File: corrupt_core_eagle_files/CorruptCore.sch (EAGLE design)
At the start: 90 parts, among them K1 DTS-3, K10 DTS-3, K11 DTS-3, K12 DTS-3, K13 DTS-3, K14 DTS-3, K15 DTS-3, K16 DTS-3, K2 DTS-3, K3 DTS-3, K4 DTS-3, K5 DTS-3, K6 DTS-3, K7 DTS-3, K8 DTS-3, K9 DTS-3, T1 TRANS_NPN-MMBTA42, T2 TRANS_NPN-MMBTA42, T3 TRANS_NPN-MMBTA42, T4 TRANS_NPN-MMBTA42, U1 MEGA8-P, U2 SNX4HC595SOIC16, U3 SNX4HC595SOIC16, U4 SNX4HC595SOIC16, U5 ULN2803ASOIC18, U6 ULN2803ASOIC18, U7 ULN2803ASOIC18, U8 LTC1799, Y1 16MHz

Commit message: -routed everything
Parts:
- added DUMMY@PROG: DUMMY, wirepad:1,6/0,8
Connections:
- net GND: now also DUMMY@PROG.P
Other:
- moved on the sheet: 5V@POT1, 5V@POT2, 5V@POT3, GND@POT1, GND@POT2, GND@POT3, POT1, POT2, POT3, RESET, RX, TX
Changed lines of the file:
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@@
 <part name="CPT1" library="wirepad" library_urn="urn:adsk.eagle:library:412" deviceset="1,6/0,8" device=""/>
 <part name="P+17" library="supply1" library_urn="urn:adsk.eagle:library:371" deviceset="+5V" device=""/>
+<part name="DUMMY@PROG" library="wirepad" library_urn="urn:adsk.eagle:library:412" deviceset="1,6/0,8" device="" value="DUMMY"/>
+<part name="GND17" library="supply1" library_urn="urn:adsk.eagle:library:371" deviceset="GND" device=""/>
 </parts>
 <sheets>
@@
 <instance part="GND34" gate="1" x="-10.16" y="35.56"/>
 <instance part="P+10" gate="1" x="7.62" y="43.18"/>
-<instance part="TX" gate="P" x="35.56" y="-33.02" rot="R180"/>
-<instance part="RX" gate="P" x="35.56" y="-38.1" rot="R180"/>
-<instance part="RESET" gate="P" x="35.56" y="-43.18" rot="R180"/>
+<instance part="TX" gate="P" x="35.56" y="-35.56" rot="R180"/>
+<instance part="RX" gate="P" x="35.56" y="-40.64" rot="R180"/>
+<instance part="RESET" gate="P" x="35.56" y="-45.72" rot="R180"/>
 <instance part="5V@PROG" gate="P" x="43.18" y="-30.48"/>
 <instance part="GND@PROG" gate="P" x="43.18" y="-40.64"/>
 <instance part="GND35" gate="1" x="60.96" y="-40.64" rot="R90"/>
 <instance part="P+11" gate="1" x="60.96" y="-30.48" rot="R270"/>
-<instance part="GND@POT1" gate="P" x="15.24" y="-55.88"/>
-<instance part="5V@POT1" gate="P" x="15.24" y="-60.96"/>
-<instance part="POT1" gate="P" x="15.24" y="-66.04"/>
-<instance part="GND@POT2" gate="P" x="43.18" y="-55.88"/>
-<instance part="5V@POT2" gate="P" x="43.18" y="-60.96"/>
-<instance part="POT2" gate="P" x="43.18" y="-66.04"/>
-<instance part="POT3" gate="P" x="71.12" y="-66.04"/>
-<instance part="5V@POT3" gate="P" x="71.12" y="-60.96"/>
-<instance part="GND@POT3" gate="P" x="71.12" y="-55.88"/>
-<instance part="GND36" gate="1" x="86.36" y="-55.88" rot="R90"/>
-<instance part="GND37" gate="1" x="58.42" y="-55.88" rot="R90"/>
-<instance part="GND38" gate="1" x="30.48" y="-55.88" rot="R90"/>
-<instance part="P+12" gate="1" x="93.98" y="-60.96" rot="R270"/>
-<instance part="P+13" gate="1" x="66.04" y="-60.96" rot="R270"/>
-<instance part="P+14" gate="1" x="38.1" y="-60.96" rot="R270"/>
+<instance part="GND@POT1" gate="P" x="15.24" y="-63.5"/>
+<instance part="5V@POT1" gate="P" x="15.24" y="-68.58"/>
+<instance part="POT1" gate="P" x="15.24" y="-73.66"/>
+<instance part="GND@POT2" gate="P" x="43.18" y="-63.5"/>
+<instance part="5V@POT2" gate="P" x="43.18" y="-68.58"/>
+<instance part="POT2" gate="P" x="43.18" y="-73.66"/>
+<instance part="POT3" gate="P" x="71.12" y="-73.66"/>
+<instance part="5V@POT3" gate="P" x="71.12" y="-68.58"/>
+<instance part="GND@POT3" gate="P" x="71.12" y="-63.5"/>
+<instance part="GND36" gate="1" x="86.36" y="-63.5" rot="R90"/>
+<instance part="GND37" gate="1" x="58.42" y="-63.5" rot="R90"/>
+<instance part="GND38" gate="1" x="30.48" y="-63.5" rot="R90"/>
+<instance part="P+12" gate="1" x="93.98" y="-68.58" rot="R270"/>
+<instance part="P+13" gate="1" x="66.04" y="-68.58" rot="R270"/>
+<instance part="P+14" gate="1" x="38.1" y="-68.58" rot="R270"/>
 <instance part="T1" gate="G$1" x="276.86" y="-38.1" rot="MR180"/>
 <instance part="T2" gate="G$1" x="276.86" y="-5.08" rot="MR180"/>
@@
 <instance part="CPT1" gate="P" x="330.2" y="-43.18" rot="R270"/>
 <instance part="P+17" gate="1" x="330.2" y="-50.8" rot="MR180"/>
+<instance part="DUMMY@PROG" gate="P" x="43.18" y="-50.8"/>
+<instance part="GND17" gate="1" x="60.96" y="-50.8" rot="R90"/>
 </instances>
 <busses>
@@
 <segment>
 <pinref part="5V@POT3" gate="P" pin="P"/>
-<wire x1="73.66" y1="-60.96" x2="91.44" y2="-60.96" width="0.1524" layer="91"/>
+<wire x1="73.66" y1="-68.58" x2="91.44" y2="-68.58" width="0.1524" layer="91"/>
 <pinref part="P+12" gate="1" pin="+5V"/>
 </segment>
 <segment>
 <pinref part="5V@POT2" gate="P" pin="P"/>
-<wire x1="45.72" y1="-60.96" x2="63.5" y2="-60.96" width="0.1524" layer="91"/>
+<wire x1="45.72" y1="-68.58" x2="63.5" y2="-68.58" width="0.1524" layer="91"/>
 <pinref part="P+13" gate="1" pin="+5V"/>
 </segment>
 <segment>
 <pinref part="5V@POT1" gate="P" pin="P"/>
-<wire x1="17.78" y1="-60.96" x2="35.56" y2="-60.96" width="0.1524" layer="91"/>
+<wire x1="17.78" y1="-68.58" x2="35.56" y2="-68.58" width="0.1524" layer="91"/>
 <pinref part="P+14" gate="1" pin="+5V"/>
 </segment>
@@
 <segment>
 <pinref part="GND@POT3" gate="P" pin="P"/>
-<wire x1="73.66" y1="-55.88" x2="83.82" y2="-55.88" width="0.1524" layer="91"/>
+<wire x1="73.66" y1="-63.5" x2="83.82" y2="-63.5" width="0.1524" layer="91"/>
 <pinref part="GND36" gate="1" pin="GND"/>
 </segment>
 <segment>
 <pinref part="GND@POT2" gate="P" pin="P"/>
-<wire x1="45.72" y1="-55.88" x2="55.88" y2="-55.88" width="0.1524" layer="91"/>
+<wire x1="45.72" y1="-63.5" x2="55.88" y2="-63.5" width="0.1524" layer="91"/>
 <pinref part="GND37" gate="1" pin="GND"/>
 </segment>
 <segment>
 <pinref part="GND@POT1" gate="P" pin="P"/>
-<wire x1="17.78" y1="-55.88" x2="27.94" y2="-55.88" width="0.1524" layer="91"/>
+<wire x1="17.78" y1="-63.5" x2="27.94" y2="-63.5" width="0.1524" layer="91"/>
 <pinref part="GND38" gate="1" pin="GND"/>
 </segment>
@@
 <wire x1="320.04" y1="0" x2="317.5" y2="0" width="0.1524" layer="91"/>
 <junction x="317.5" y="0"/>
+</segment>
+<segment>
+<pinref part="DUMMY@PROG" gate="P" pin="P"/>
+<pinref part="GND17" gate="1" pin="GND"/>
+<wire x1="45.72" y1="-50.8" x2="58.42" y2="-50.8" width="0.1524" layer="91"/>
 </segment>
 </net>
@@
 <segment>
 <pinref part="RESET" gate="P" pin="P"/>
-<wire x1="33.02" y1="-43.18" x2="27.94" y2="-43.18" width="0.1524" layer="91"/>
-<junction x="27.94" y="-43.18"/>
-<label x="27.94" y="-43.18" size="1.778" layer="95" rot="R180"/>
+<wire x1="33.02" y1="-45.72" x2="27.94" y2="-45.72" width="0.1524" layer="91"/>
+<junction x="27.94" y="-45.72"/>
+<label x="27.94" y="-45.72" size="1.778" layer="95" rot="R180"/>
 </segment>
 </net>
@@
 <segment>
 <pinref part="RX" gate="P" pin="P"/>
-<wire x1="33.02" y1="-38.1" x2="27.94" y2="-38.1" width="0.1524" layer="91"/>
-<junction x="27.94" y="-38.1"/>
-<label x="27.94" y="-38.1" size="1.778" layer="95" rot="R180"/>
+<wire x1="33.02" y1="-40.64" x2="27.94" y2="-40.64" width="0.1524" layer="91"/>
+<junction x="27.94" y="-40.64"/>
+<label x="27.94" y="-40.64" size="1.778" layer="95" rot="R180"/>
 </segment>
 </net>
@@
 <segment>
 <pinref part="TX" gate="P" pin="P"/>
-<wire x1="33.02" y1="-33.02" x2="27.94" y2="-33.02" width="0.1524" layer="91"/>
-<junction x="27.94" y="-33.02"/>
-<label x="27.94" y="-33.02" size="1.778" layer="95" rot="R180"/>
+<wire x1="33.02" y1="-35.56" x2="27.94" y2="-35.56" width="0.1524" layer="91"/>
+<junction x="27.94" y="-35.56"/>
+<label x="27.94" y="-35.56" size="1.778" layer="95" rot="R180"/>
 </segment>
 </net>
@@
 <segment>
 <pinref part="POT3" gate="P" pin="P"/>
-<wire x1="73.66" y1="-66.04" x2="81.28" y2="-66.04" width="0.1524" layer="91"/>
-<junction x="81.28" y="-66.04"/>
-<label x="81.28" y="-66.04" size="1.778" layer="95"/>
+<wire x1="73.66" y1="-73.66" x2="81.28" y2="-73.66" width="0.1524" layer="91"/>
+<junction x="81.28" y="-73.66"/>
+<label x="81.28" y="-73.66" size="1.778" layer="95"/>
 </segment>
 </net>
@@
 <segment>
 <pinref part="POT1" gate="P" pin="P"/>
-<wire x1="17.78" y1="-66.04" x2="25.4" y2="-66.04" width="0.1524" layer="91"/>
-<junction x="25.4" y="-66.04"/>
-<label x="25.4" y="-66.04" size="1.778" layer="95"/>
+<wire x1="17.78" y1="-73.66" x2="25.4" y2="-73.66" width="0.1524" layer="91"/>
+<junction x="25.4" y="-73.66"/>
+<label x="25.4" y="-73.66" size="1.778" layer="95"/>
 </segment>
 </net>
@@
 <segment>
 <pinref part="POT2" gate="P" pin="P"/>
-<wire x1="45.72" y1="-66.04" x2="53.34" y2="-66.04" width="0.1524" layer="91"/>
-<junction x="53.34" y="-66.04"/>
-<label x="53.34" y="-66.04" size="1.778" layer="95"/>
-</segment>
-</net>
+<wire x1="45.72" y1="-73.66" x2="53.34" y2="-73.66" width="0.1524" layer="91"/>
+<junction x="53.34" y="-73.66"/>
+<label x="53.34" y="-73.66" size="1.778" layer="95"/>
+</segment>
+</net>

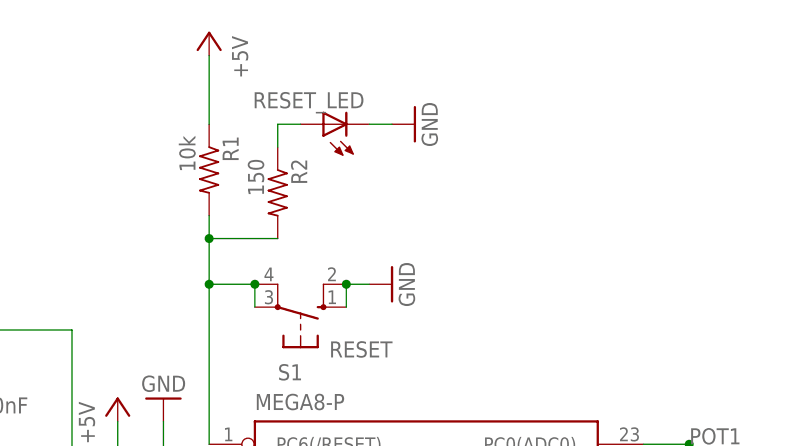
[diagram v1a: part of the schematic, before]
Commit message: -I was a dummy and wired up the RESET status LED wrong, causing a voltage drop that held the RESET line low no matter what. I fixed it so it just uses a transistor to control the RESET LED.
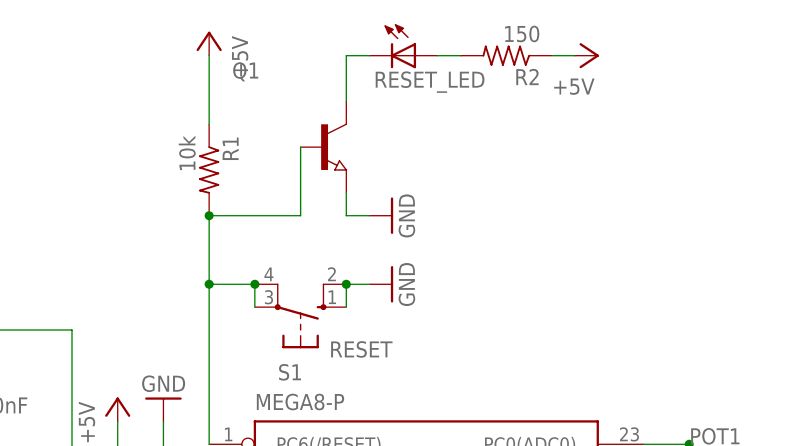
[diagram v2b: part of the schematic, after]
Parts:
- added Q1: (no value), semicon-smd-ipc:NPN-TRANSISTOR_SOT23
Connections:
- new net N$17: Q1.C, RESET_LED.C
- net +5V: now also R2.1
- net GND: now also Q1.E; no longer RESET_LED.C
- net N$6: now also R2.2; no longer R2.1
- net RESET: now also Q1.B; no longer R2.2
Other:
- moved on the sheet: R2, RESET_LED
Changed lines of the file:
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@@
 <part name="DUMMY@PROG" library="wirepad" library_urn="urn:adsk.eagle:library:412" deviceset="1,6/0,8" device="" value="DUMMY"/>
 <part name="GND17" library="supply1" library_urn="urn:adsk.eagle:library:371" deviceset="GND" device=""/>
+<part name="Q1" library="semicon-smd-ipc" library_urn="urn:adsk.eagle:library:353" deviceset="NPN-TRANSISTOR_" device="SOT23" package3d_urn="urn:adsk.eagle:package:26310/1"/>
+<part name="P+18" library="supply1" library_urn="urn:adsk.eagle:library:371" deviceset="+5V" device=""/>
 </parts>
 <sheets>
@@
 <instance part="K16" gate="G$1" x="370.84" y="25.4" rot="R270"/>
 <instance part="PWR_LED" gate="G$1" x="15.24" y="-17.78"/>
-<instance part="RESET_LED" gate="G$1" x="30.48" y="73.66" rot="R90"/>
-<instance part="R2" gate="G$1" x="25.4" y="66.04" rot="R270"/>
+<instance part="RESET_LED" gate="G$1" x="40.64" y="81.28" rot="R270"/>
+<instance part="R2" gate="G$1" x="50.8" y="81.28" rot="R180"/>
 <instance part="R3" gate="G$1" x="15.24" y="-5.08" rot="R90"/>
 <instance part="GND31" gate="1" x="15.24" y="-27.94"/>
-<instance part="GND32" gate="1" x="40.64" y="73.66" rot="R90"/>
+<instance part="GND32" gate="1" x="38.1" y="63.5" rot="R90"/>
 <instance part="C3" gate="G$1" x="5.08" y="-2.54"/>
 <instance part="GND33" gate="1" x="5.08" y="-12.7"/>
@@
 <instance part="DUMMY@PROG" gate="P" x="43.18" y="-50.8"/>
 <instance part="GND17" gate="1" x="60.96" y="-50.8" rot="R90"/>
+<instance part="Q1" gate="G$1" x="30.48" y="71.12"/>
+<instance part="P+18" gate="1" x="60.96" y="81.28" rot="MR90"/>
 </instances>
 <busses>
@@
 <pinref part="P+17" gate="1" pin="+5V"/>
 </segment>
+<segment>
+<pinref part="P+18" gate="1" pin="+5V"/>
+<pinref part="R2" gate="G$1" pin="1"/>
+<wire x1="58.42" y1="81.28" x2="55.88" y2="81.28" width="0.1524" layer="91"/>
+</segment>
 </net>
 <net name="GND" class="0">
@@
 <pinref part="GND31" gate="1" pin="GND"/>
 <wire x1="15.24" y1="-25.4" x2="15.24" y2="-22.86" width="0.1524" layer="91"/>
-</segment>
-<segment>
-<pinref part="RESET_LED" gate="G$1" pin="C"/>
-<pinref part="GND32" gate="1" pin="GND"/>
-<wire x1="35.56" y1="73.66" x2="38.1" y2="73.66" width="0.1524" layer="91"/>
 </segment>
 <segment>
@@
 <wire x1="45.72" y1="-50.8" x2="58.42" y2="-50.8" width="0.1524" layer="91"/>
 </segment>
+<segment>
+<pinref part="Q1" gate="G$1" pin="E"/>
+<wire x1="33.02" y1="66.04" x2="33.02" y2="63.5" width="0.1524" layer="91"/>
+<pinref part="GND32" gate="1" pin="GND"/>
+<wire x1="33.02" y1="63.5" x2="35.56" y2="63.5" width="0.1524" layer="91"/>
+</segment>
 </net>
 <net name="RESET" class="0">
@@
 <pinref part="R1" gate="G$1" pin="2"/>
 <pinref part="U1" gate="G$1" pin="PC6(/RESET)"/>
-<wire x1="17.78" y1="63.5" x2="17.78" y2="60.96" width="0.1524" layer="91"/>
-<wire x1="17.78" y1="60.96" x2="17.78" y2="55.88" width="0.1524" layer="91"/>
+<wire x1="17.78" y1="63.5" x2="17.78" y2="55.88" width="0.1524" layer="91"/>
 <wire x1="17.78" y1="55.88" x2="17.78" y2="38.1" width="0.1524" layer="91"/>
 <pinref part="S1" gate="1" pin="P1"/>
@@
 <pinref part="S1" gate="1" pin="P"/>
 <junction x="22.86" y="55.88"/>
-<wire x1="17.78" y1="60.96" x2="25.4" y2="60.96" width="0.1524" layer="91"/>
-<junction x="17.78" y="60.96"/>
-<pinref part="R2" gate="G$1" pin="2"/>
 <wire x1="22.86" y1="53.34" x2="22.86" y2="55.88" width="0.1524" layer="91"/>
+<wire x1="17.78" y1="63.5" x2="27.94" y2="63.5" width="0.1524" layer="91"/>
+<junction x="17.78" y="63.5"/>
+<pinref part="Q1" gate="G$1" pin="B"/>
+<wire x1="27.94" y1="63.5" x2="27.94" y2="71.12" width="0.1524" layer="91"/>
 </segment>
 <segment>
@@
 </segment>
 </net>
-<net name="N$6" class="0">
-<segment>
-<pinref part="R2" gate="G$1" pin="1"/>
-<pinref part="RESET_LED" gate="G$1" pin="A"/>
-<wire x1="25.4" y1="71.12" x2="25.4" y2="73.66" width="0.1524" layer="91"/>
-<wire x1="25.4" y1="73.66" x2="27.94" y2="73.66" width="0.1524" layer="91"/>
-</segment>
-</net>
 <net name="N$7" class="0">
 <segment>
@@
 <pinref part="CPT2" gate="P" pin="P"/>
 <wire x1="330.2" y1="-35.56" x2="330.2" y2="-33.02" width="0.1524" layer="91"/>
+</segment>
+</net>
+<net name="N$6" class="0">
+<segment>
+<pinref part="RESET_LED" gate="G$1" pin="A"/>
+<pinref part="R2" gate="G$1" pin="2"/>
+<wire x1="43.18" y1="81.28" x2="45.72" y2="81.28" width="0.1524" layer="91"/>
+</segment>
+</net>
+<net name="N$17" class="0">
+<segment>
+<pinref part="Q1" gate="G$1" pin="C"/>
+<wire x1="33.02" y1="76.2" x2="33.02" y2="81.28" width="0.1524" layer="91"/>
+<pinref part="RESET_LED" gate="G$1" pin="C"/>
+<wire x1="33.02" y1="81.28" x2="35.56" y2="81.28" width="0.1524" layer="91"/>
 </segment>
 </net>
@@
 with this version.
 </note>
+<note version="8.3" severity="warning">
+Since Version 8.3, EAGLE supports URNs for individual library
+assets (packages, symbols, and devices). The URNs of those assets
+will not be understood (or retained) with this version.
+</note>
+<note version="8.3" severity="warning">
+Since Version 8.3, EAGLE supports the association of 3D packages
+with devices in libraries, schematics, and board files. Those 3D
+packages will not be understood (or retained) with this version.
+</note>
 </compatibility>
